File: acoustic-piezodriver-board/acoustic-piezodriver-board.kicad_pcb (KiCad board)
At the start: 4 copper layers, 100 x 62 mm, 160 parts, among them J301 Conn_02x06_Odd_Even, J501 Conn_02x06_Odd_Even, P101 WJ128V-5.0-3P, P201 WJ128V-5.0-3P, Q501 AO3400A, Q502 AO3400A, U10 NCE6005AS, U101 AMS1117-3.3, U102 TMCS1108A3UQDR, U201 UCC27282DR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

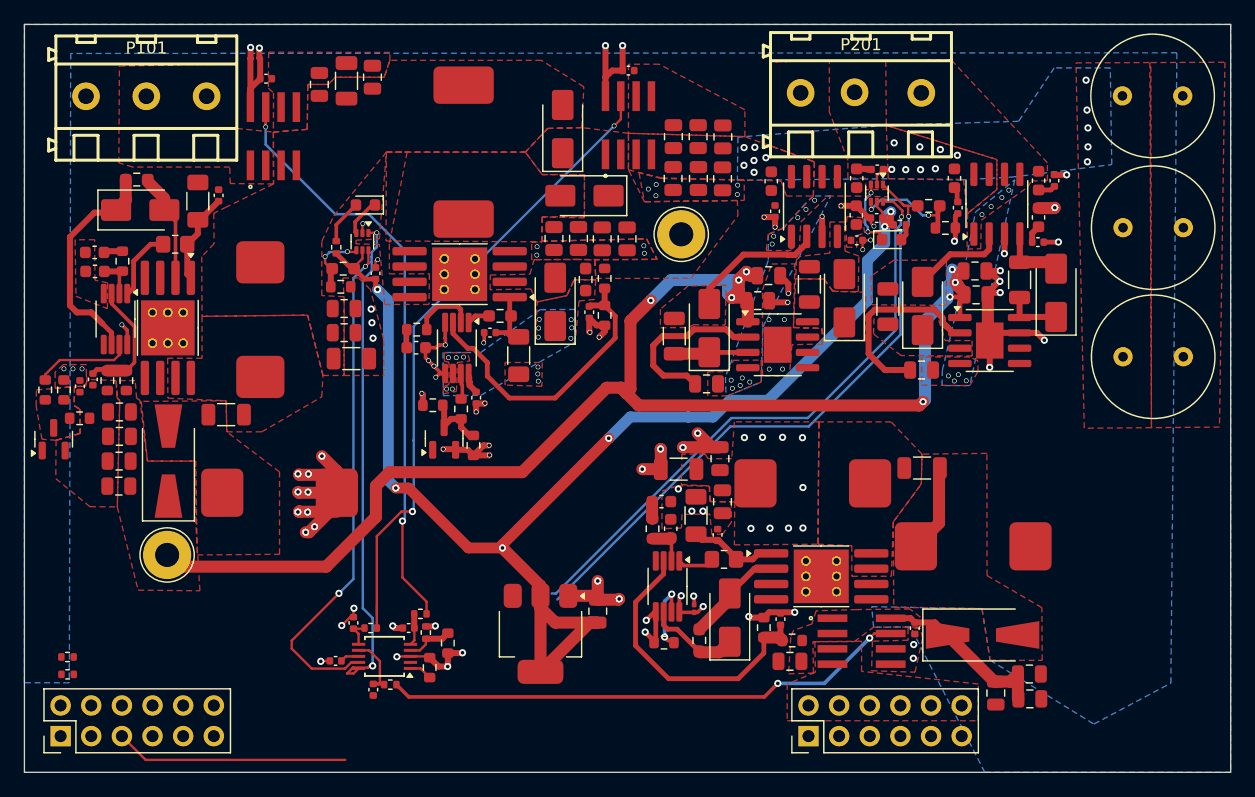
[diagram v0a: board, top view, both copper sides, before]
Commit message: Fixed ERC, DRC errors, finished routing (next) perform footprint checks
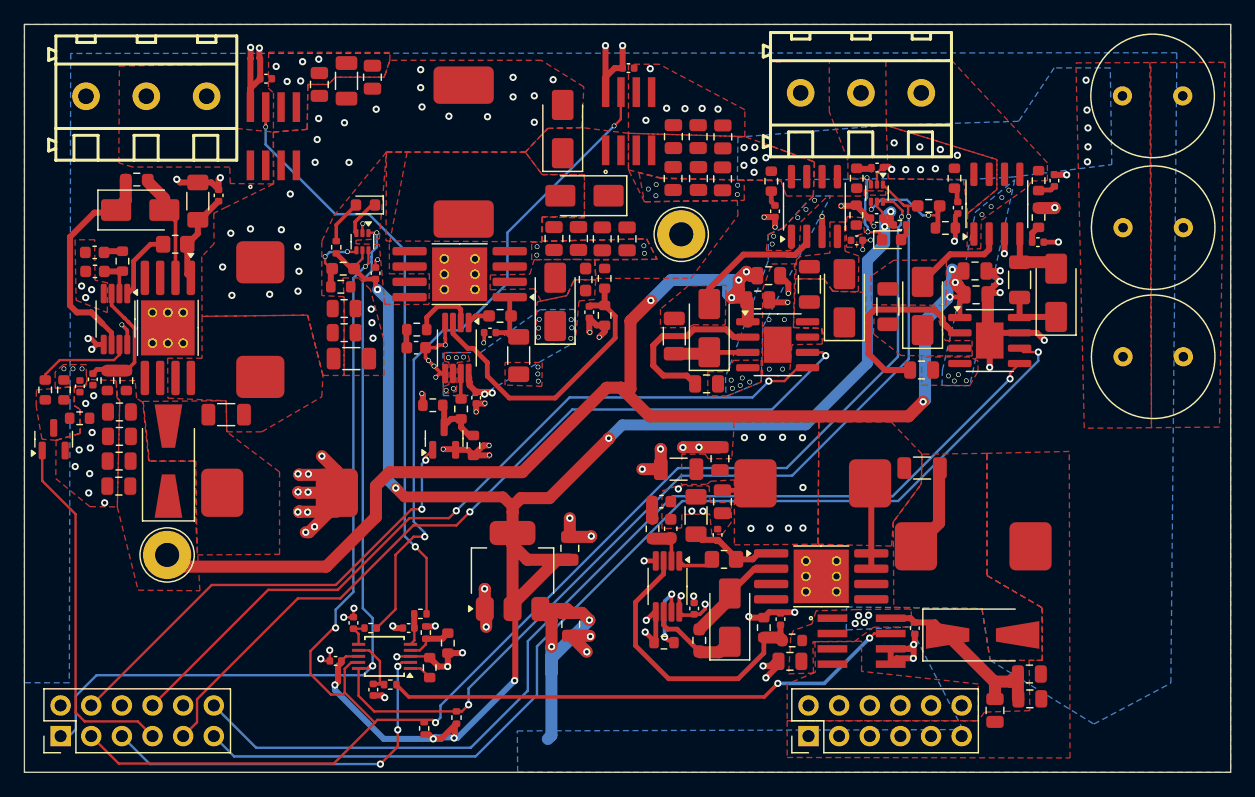
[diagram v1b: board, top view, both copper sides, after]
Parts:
- added C103: 1uF, Capacitor_SMD:C_0805_2012Metric, F.Cu at (89.3, 129.7)
- C301: footprint Capacitor_SMD:C_0201_0603Metric -> Capacitor_SMD:C_0402_1005Metric
- D401, D402: footprint Diode_SMD:D_0603_1608Metric -> LED_SMD:LED_0603_1608Metric
- R10, R5, R6, R7, R8, R9: footprint Capacitor_SMD:C_0603_1608Metric -> Resistor_SMD:R_0603_1608Metric
- moved R404 32.4 mm to (79.8, 137.5), turned to -90 degrees
- moved R403 30.2 mm to (77.1, 138.4), turned to -90 degrees
- moved U101 5.70 mm to (84.5, 125.3), turned to 90 degrees
- moved C101 5.70 mm to (89.2, 123.4)
- moved C42 1.44 mm to (124.5, 136.9)
- moved U204 0.34 mm to (94.1, 88.0)
- moved C210 0.20 mm to (94.1, 83.6)
- moved C8 0.16 mm to (114.7, 91.9)
- moved C4 0.06 mm to (104.8, 102.8)
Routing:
- net /INVERTER/PWM.0_LI: track 0.00 -> 87.4 mm, vias 0 -> 1
- net /INVERTER/PWM.0_HI: track 0.00 -> 84.1 mm, vias 0 -> 1
- net /INVERTER/PWM.1_LI: track 0.00 -> 69.1 mm, vias 0 -> 2
- net /INVERTER/PWM.1_HI: track 0.00 -> 65.9 mm, vias 0 -> 2
- net /SENSORS_CONN/T_SCL: track 93.6 -> 146.7 mm, vias 3 -> 4
- net /SENSORS_CONN/T_SDA: track 91.7 -> 144.3 mm, vias 3 -> 4
- net /INVERTER/PBOOST_EN: track 0.00 -> 39.5 mm, vias 0 -> 2
- net /INVERTER/PSEPIC_EN: track 0.00 -> 30.0 mm
- net +3V3: track 113.5 -> 143.0 mm, vias 6 -> 9
- net +6V: track 33.2 -> 59.6 mm, vias 4 -> 10
- net GND: track 111.9 -> 136.5 mm, vias 85 -> 121
- net /SENSORS_CONN/ADC_ALERT: track 19.3 -> 32.3 mm, vias 0 -> 3
- net Net-(C38-Pad1): track 0.14 -> 7.26 mm
- net +BATT: track 8.69 -> 14.5 mm, vias 17 -> 45
- net /INVERTER/10V: track 117.4 -> 119.0 mm
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
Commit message: changed footprints,  changed stackup from L3:PWR-> L3:GND and routed +BATT on 4th layer
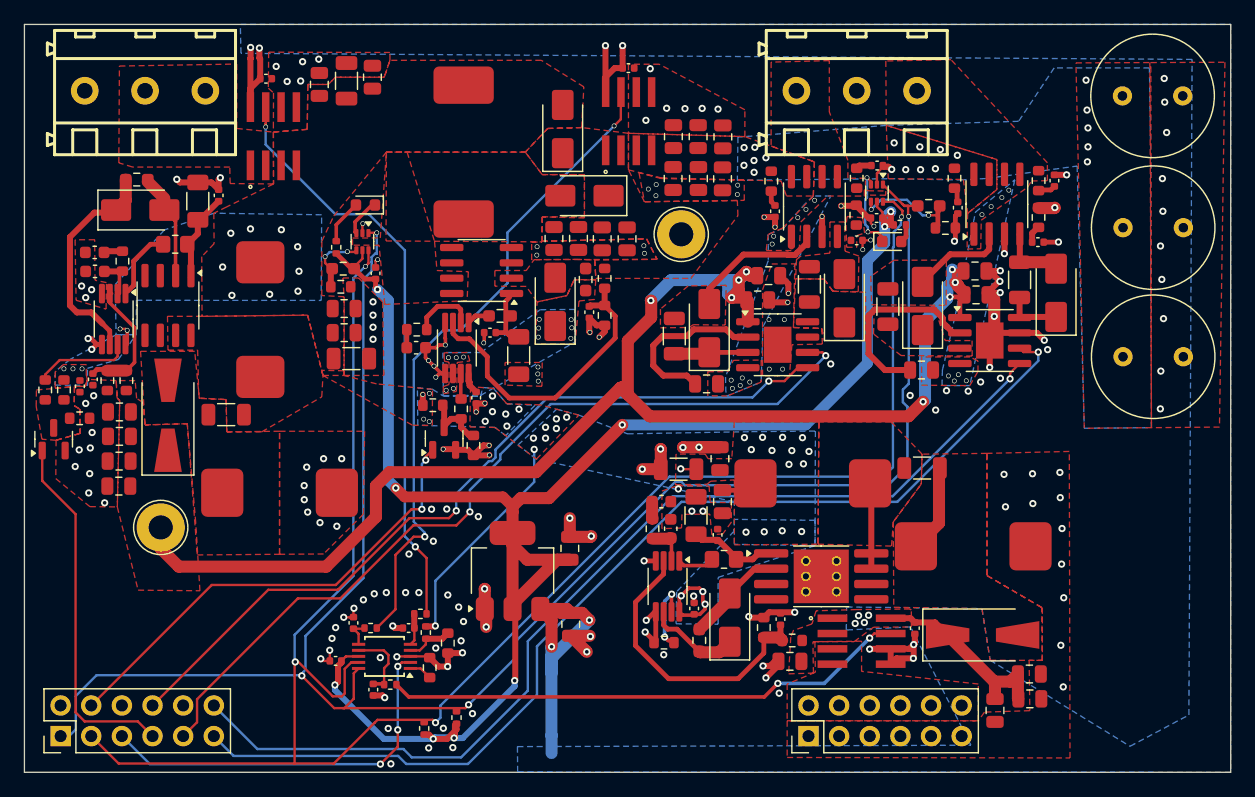
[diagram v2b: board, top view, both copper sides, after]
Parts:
- U501, U503: footprint Package_SO:SOP-8-1EP_4.57x4.57mm_P1.27mm_EP4.57x4.45mm_ThermalVias -> Package_SO:SOIC-8_3.9x4.9mm_P1.27mm
- moved D502 3.80 mm to (55.9, 112.4)
- moved TP502 2.34 mm to (55.3, 121.7)
- moved U501 1.86 mm to (55.9, 103.3)
- moved U503 1.85 mm to (81.9, 100.4)
- moved P101 0.47 mm to (54.0, 85.5)
- moved P201 0.39 mm to (113.0, 85.5)
- moved C8 0.17 mm to (114.7, 91.7)
- moved D402 0.16 mm to (115.9, 98.0)
- moved U502 0.15 mm to (51.4, 104.4)
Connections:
- net /INVERTER/10V renamed /INVERTER/+10V
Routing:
- net +BATT: track 14.5 -> 35.2 mm, vias 45 -> 50
- net GND: track 136.5 -> 121.4 mm, vias 121 -> 178
- net /SENSORS_CONN/T_SDA: track 144.3 -> 155.9 mm
- net /SENSORS_CONN/T_SCL: track 146.7 -> 154.4 mm
- net /INVERTER/+10V: track 119.0 -> 121.8 mm
- net /INVERTER/PWM.1_LI: track 69.1 -> 70.4 mm
- net /INVERTER/PWM.1_HI: track 65.9 -> 67.1 mm
- net +6V: track 59.6 -> 60.6 mm
- net /INVERTER/PWM.0_HI: track 84.1 -> 84.8 mm
- net Net-(U404-AIN3): track 5.50 -> 6.16 mm
- net +3V3: track 143.0 -> 143.5 mm
- net /INVERTER/PWM.0_LI: track 87.4 -> 87.9 mm
- added copper zone on B.Cu, net +BATT
- added copper zone on In2.Cu, net GND
- removed copper zone on In2.Cu, net +BATT
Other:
- board text removed: "Routed driver on lower layer to avoid coupling of driver current into feedback path"

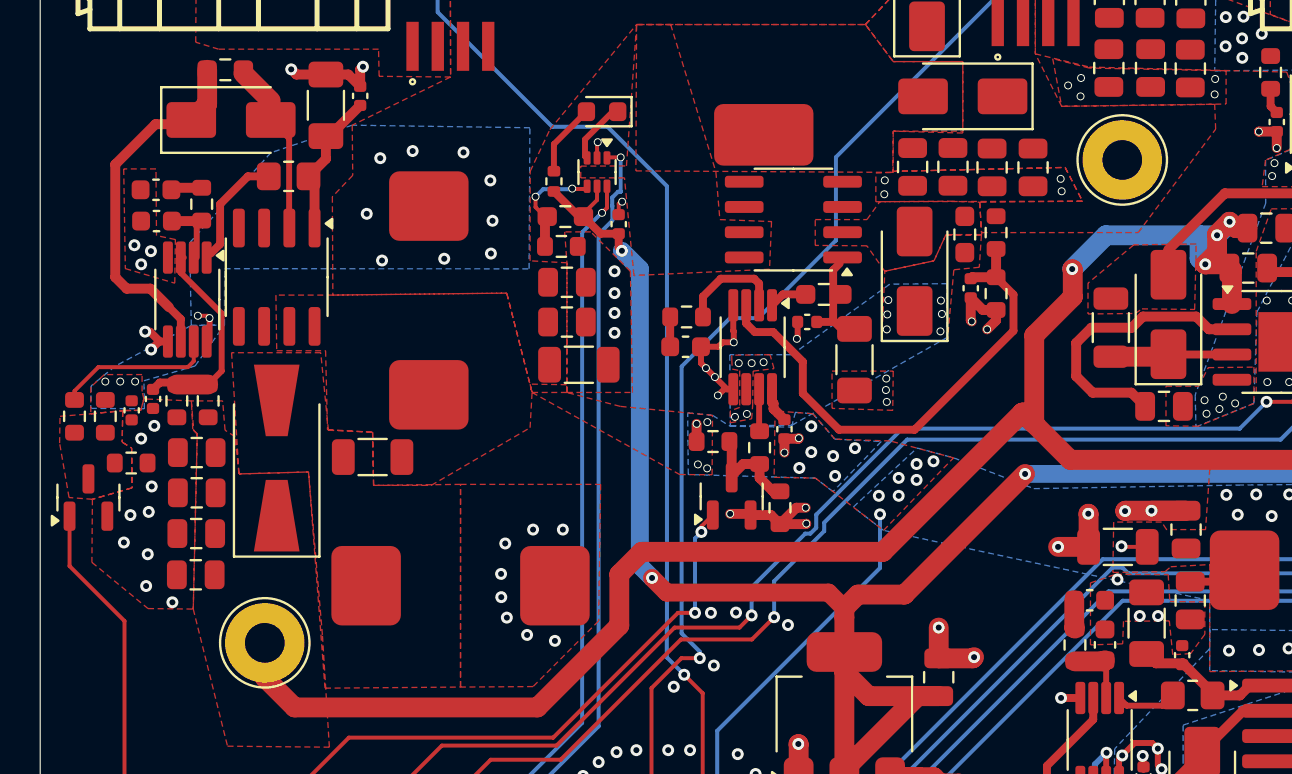
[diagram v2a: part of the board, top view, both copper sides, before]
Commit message: [production checks] checked caps, [todo] Think about replacing 220 nF filtering caps in DC-DC to 0402 package (next) check rest of footprints
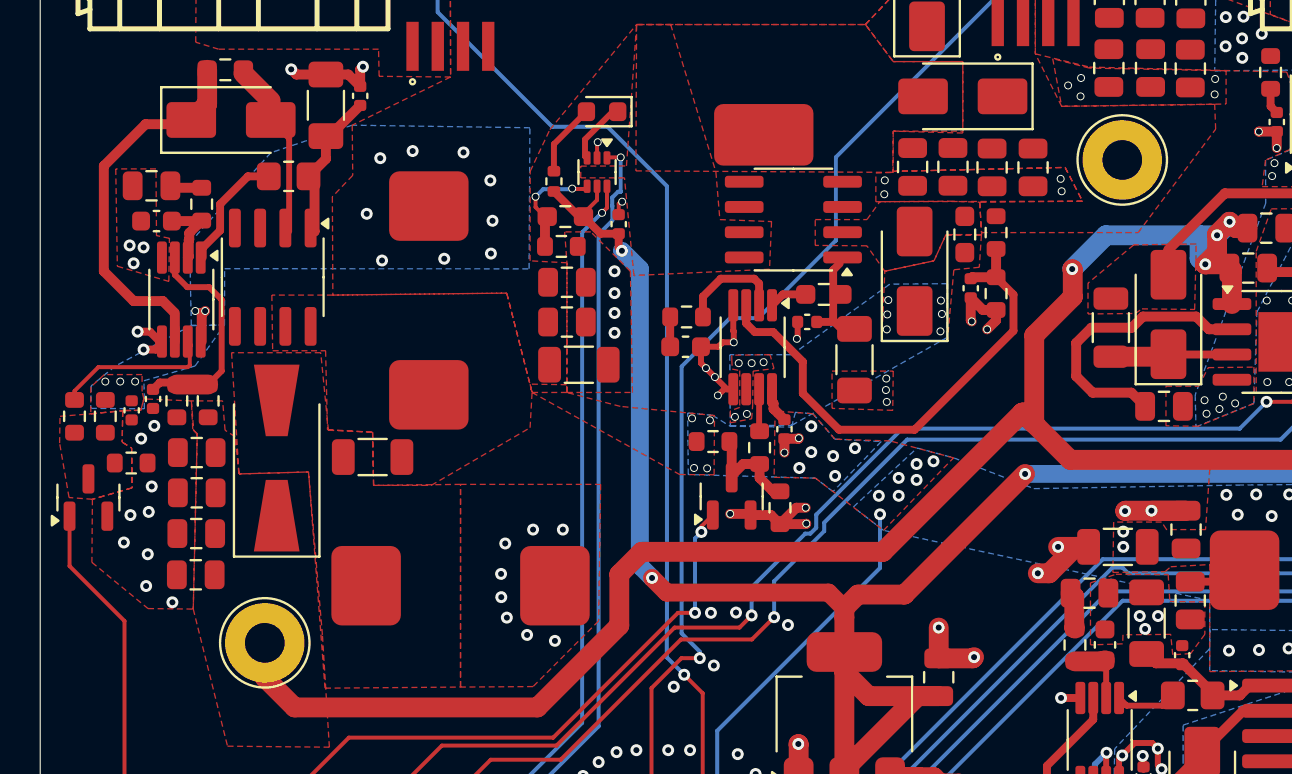
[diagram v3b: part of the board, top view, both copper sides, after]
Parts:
- C32, C509: footprint Capacitor_SMD:C_0603_1608Metric -> Capacitor_SMD:C_0805_2012Metric
- moved C32 0.36 mm to (96.8, 119.2)
- moved C509 0.30 mm to (49.6, 98.7)
- moved U502 0.30 mm to (51.1, 104.4)
- moved U501 0.20 mm to (55.7, 103.3)
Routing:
- net GND: track 121.4 -> 123.3 mm
- net Net-(D503-K): track 17.4 -> 18.1 mm
- net Net-(U502-FB): track 10.6 -> 11.2 mm
- net Net-(U502-COMP): track 3.48 -> 4.02 mm
- net +BATT: track 35.2 -> 35.0 mm, vias 50 -> 51

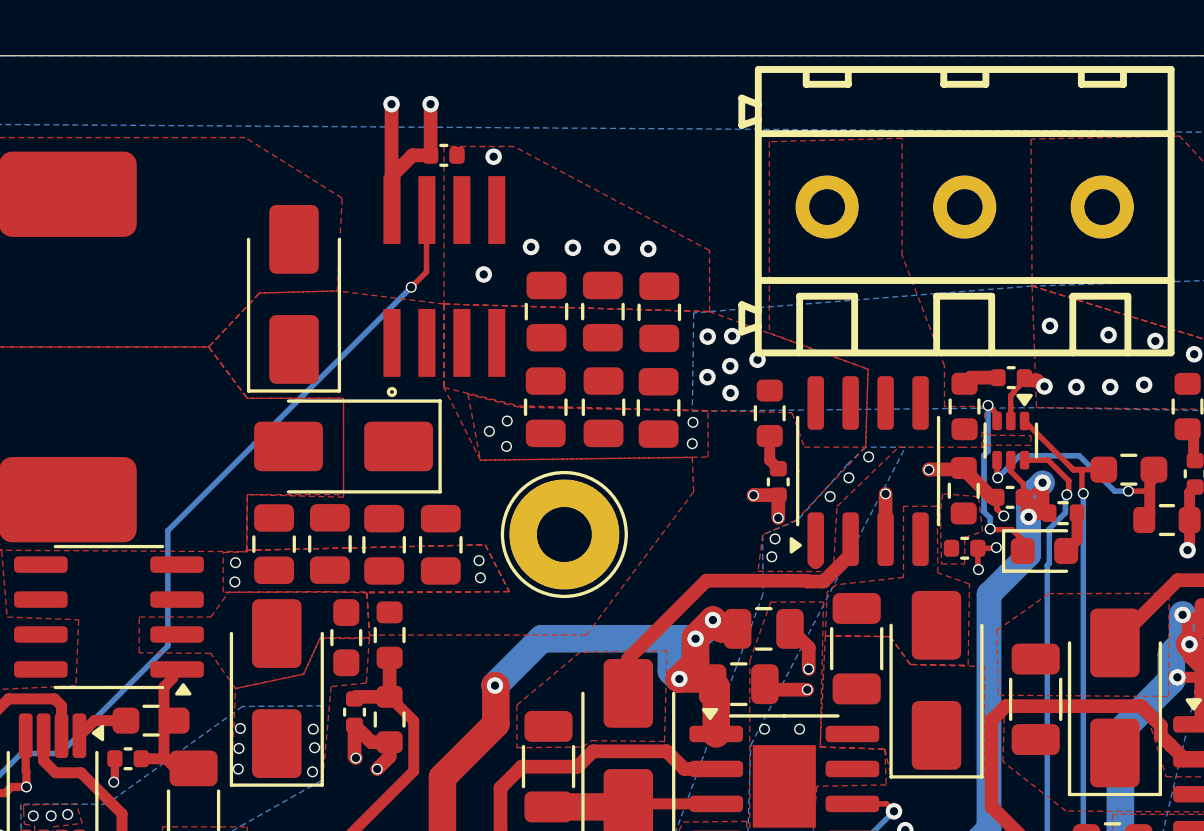
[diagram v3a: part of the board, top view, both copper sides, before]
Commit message: changed ss520 footprints
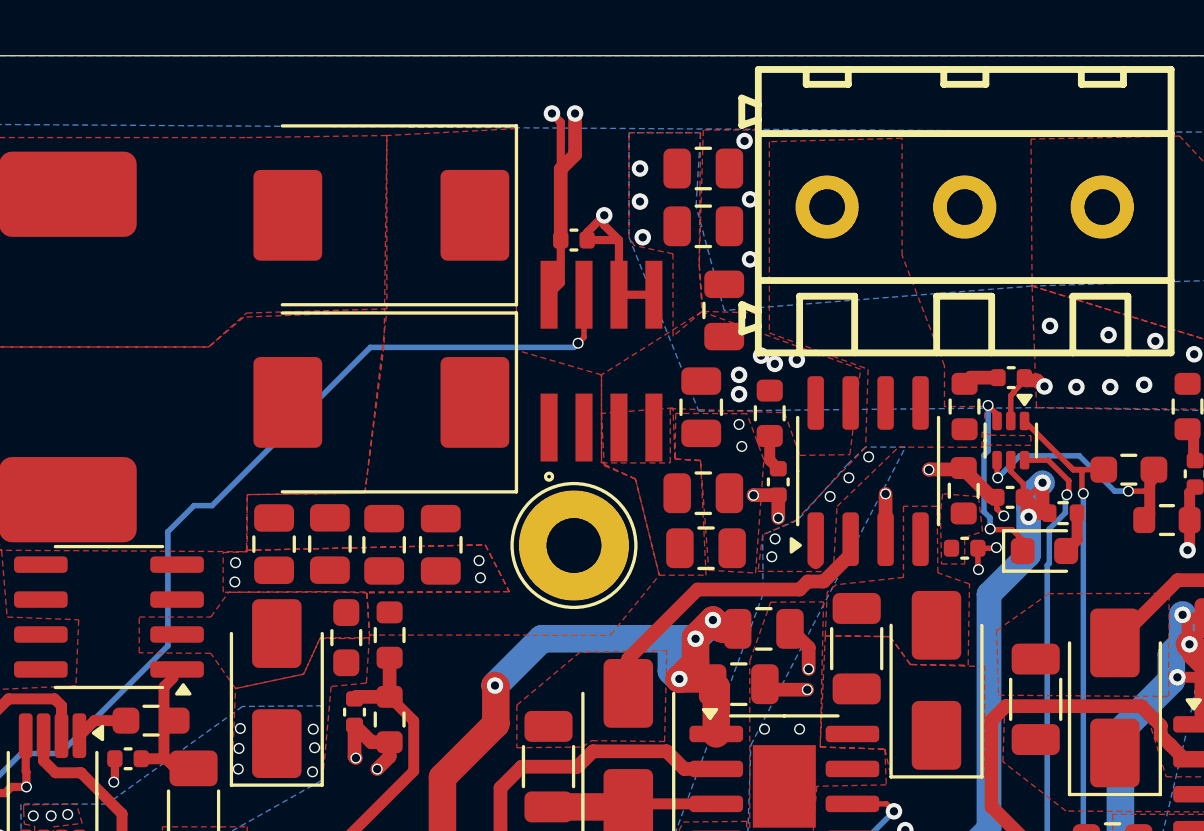
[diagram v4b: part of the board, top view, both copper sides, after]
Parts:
- D501, D504: footprint Diode_SMD:D_SMA -> Diode_SMD:D_SMC
- moved C206 7.76 mm to (103.6, 97.9), turned to 180 degrees
- moved C204 7.72 mm to (103.5, 84.1), turned to 180 degrees
- moved U204 6.49 mm to (99.8, 91.1)
- moved C210 5.64 mm to (98.8, 86.7)
- moved C209 4.79 mm to (103.5, 86.2), turned to 180 degrees
- moved C207 4.79 mm to (103.5, 95.9), turned to 180 degrees
- moved D501 4.28 mm to (91.8, 85.8), turned to 180 degrees
- moved C208 2.36 mm to (104.3, 89.3)
- moved D504 2.11 mm to (91.8, 92.6)
- moved C205 1.55 mm to (103.4, 92.8)
- moved TP501 0.53 mm to (98.8, 97.8)
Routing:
- net GND: track 123.3 -> 130.0 mm, vias 178 -> 173
- net /INVERTER/ADC_IINV: track 54.6 -> 59.0 mm
- net +6V: track 60.6 -> 64.6 mm
- net /INVERTER/VINV_N: vias 18 -> 20
